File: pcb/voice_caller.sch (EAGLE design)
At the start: 22 parts, among them IC1 PRO_MICRO, IC2 AT45DB321D-S, IC3 78L12SMD, K4 G6J-2P-Y

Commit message: All but switches
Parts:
- added C7: (no value), rcl:C-EUC1206K
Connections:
- net +3V3: now also C7.1
- net GND: now also C7.2
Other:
- moved on the sheet: C1, C2, C3
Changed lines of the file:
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@@
 <part name="R7" library="rcl" deviceset="R-EU_" device="M1206" value="1k"/>
 <part name="P+3" library="supply1" deviceset="+5V" device=""/>
+<part name="C7" library="rcl" deviceset="C-EU" device="C1206K"/>
+<part name="GND11" library="supply1" deviceset="GND" device=""/>
+<part name="+3V1" library="supply1" deviceset="+3V3" device=""/>
 </parts>
 <sheets>
@@
 </plain>
 <instances>
-<instance part="+8V" gate="VCC" x="25.4" y="99.06"/>
-<instance part="GND1" gate="1" x="25.4" y="81.28"/>
+<instance part="+8V" gate="VCC" x="147.32" y="149.86"/>
+<instance part="GND1" gate="1" x="147.32" y="132.08"/>
 <instance part="CONN_MIC" gate="G$1" x="-30.48" y="50.8" rot="MR0"/>
 <instance part="CONN_RADIO" gate="G$1" x="2.54" y="50.8"/>
-<instance part="P+2" gate="1" x="40.64" y="99.06"/>
-<instance part="GND2" gate="1" x="40.64" y="81.28"/>
-<instance part="C1" gate="G$1" x="25.4" y="91.44"/>
-<instance part="C2" gate="G$1" x="40.64" y="91.44"/>
+<instance part="P+2" gate="1" x="78.74" y="157.48"/>
+<instance part="GND2" gate="1" x="78.74" y="139.7"/>
+<instance part="C1" gate="G$1" x="147.32" y="142.24"/>
+<instance part="C2" gate="G$1" x="78.74" y="149.86"/>
 <instance part="IC2" gate="G$1" x="157.48" y="68.58"/>
-<instance part="C3" gate="G$1" x="48.26" y="91.44"/>
-<instance part="P+1" gate="1" x="48.26" y="99.06"/>
-<instance part="GND3" gate="1" x="48.26" y="81.28"/>
+<instance part="C3" gate="G$1" x="167.64" y="142.24"/>
+<instance part="P+1" gate="1" x="167.64" y="149.86"/>
+<instance part="GND3" gate="1" x="167.64" y="132.08"/>
 <instance part="IC3" gate="G$1" x="154.94" y="119.38"/>
 <instance part="R1" gate="G$1" x="-15.24" y="99.06"/>
@@
 <instance part="R7" gate="G$1" x="81.28" y="53.34"/>
 <instance part="P+3" gate="1" x="93.98" y="76.2"/>
+<instance part="C7" gate="G$1" x="190.5" y="68.58"/>
+<instance part="GND11" gate="1" x="190.5" y="58.42"/>
+<instance part="+3V1" gate="G$1" x="190.5" y="76.2"/>
 </instances>
 <busses>
@@
 <pinref part="P+2" gate="1" pin="+5V"/>
 <pinref part="C2" gate="G$1" pin="1"/>
-<wire x1="40.64" y1="93.98" x2="40.64" y2="96.52" width="0.1524" layer="91"/>
+<wire x1="78.74" y1="152.4" x2="78.74" y2="154.94" width="0.1524" layer="91"/>
 </segment>
 <segment>
 <pinref part="C3" gate="G$1" pin="1"/>
 <pinref part="P+1" gate="1" pin="+5V"/>
-<wire x1="48.26" y1="96.52" x2="48.26" y2="93.98" width="0.1524" layer="91"/>
+<wire x1="167.64" y1="147.32" x2="167.64" y2="144.78" width="0.1524" layer="91"/>
 </segment>
 <segment>
@@
 <pinref part="GND1" gate="1" pin="GND"/>
 <pinref part="C1" gate="G$1" pin="2"/>
-<wire x1="25.4" y1="83.82" x2="25.4" y2="86.36" width="0.1524" layer="91"/>
+<wire x1="147.32" y1="134.62" x2="147.32" y2="137.16" width="0.1524" layer="91"/>
 </segment>
 <segment>
 <pinref part="GND2" gate="1" pin="GND"/>
 <pinref part="C2" gate="G$1" pin="2"/>
-<wire x1="40.64" y1="83.82" x2="40.64" y2="86.36" width="0.1524" layer="91"/>
+<wire x1="78.74" y1="142.24" x2="78.74" y2="144.78" width="0.1524" layer="91"/>
 </segment>
 <segment>
@@
 <pinref part="C3" gate="G$1" pin="2"/>
 <pinref part="GND3" gate="1" pin="GND"/>
-<wire x1="48.26" y1="83.82" x2="48.26" y2="86.36" width="0.1524" layer="91"/>
+<wire x1="167.64" y1="134.62" x2="167.64" y2="137.16" width="0.1524" layer="91"/>
 </segment>
 <segment>
@@
 <wire x1="93.98" y1="45.72" x2="93.98" y2="48.26" width="0.1524" layer="91"/>
 </segment>
+<segment>
+<pinref part="GND11" gate="1" pin="GND"/>
+<pinref part="C7" gate="G$1" pin="2"/>
+<wire x1="190.5" y1="60.96" x2="190.5" y2="63.5" width="0.1524" layer="91"/>
+</segment>
 </net>
 <net name="MOSI" class="0">
@@
 <pinref part="+8V" gate="VCC" pin="VCC"/>
 <pinref part="C1" gate="G$1" pin="1"/>
-<wire x1="25.4" y1="93.98" x2="25.4" y2="96.52" width="0.1524" layer="91"/>
+<wire x1="147.32" y1="144.78" x2="147.32" y2="147.32" width="0.1524" layer="91"/>
 </segment>
 </net>
@@
 <label x="175.26" y="66.04" size="1.016" layer="95" xref="yes"/>
 </segment>
-</net>
+<segment>
+<pinref part="C7" gate="G$1" pin="1"/>
+<wire x1="190.5" y1="71.12" x2="190.5" y2="73.66" width="0.1524" layer="91"/>
+<pinref part="+3V1" gate="G$1" pin="+3V3"/>
+</segment>
+</net>

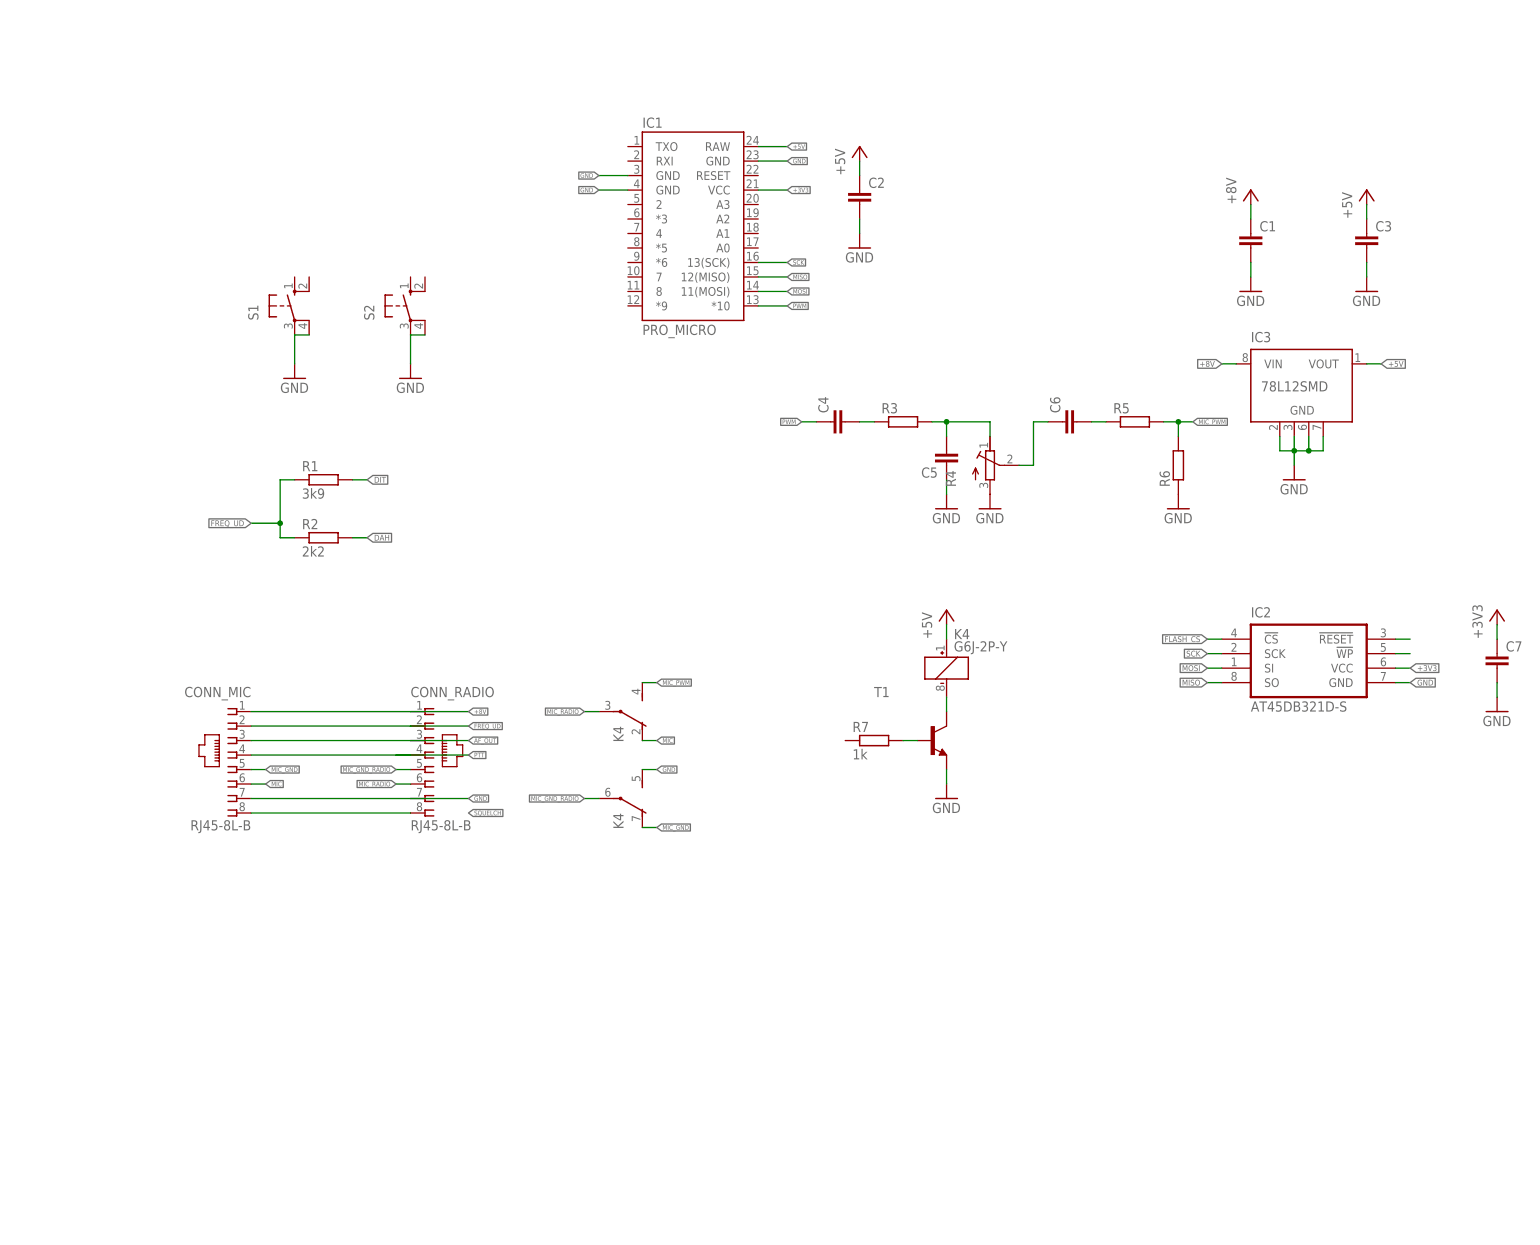
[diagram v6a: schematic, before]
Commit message: Buttons and bistable relay added, PTT thing is missing.
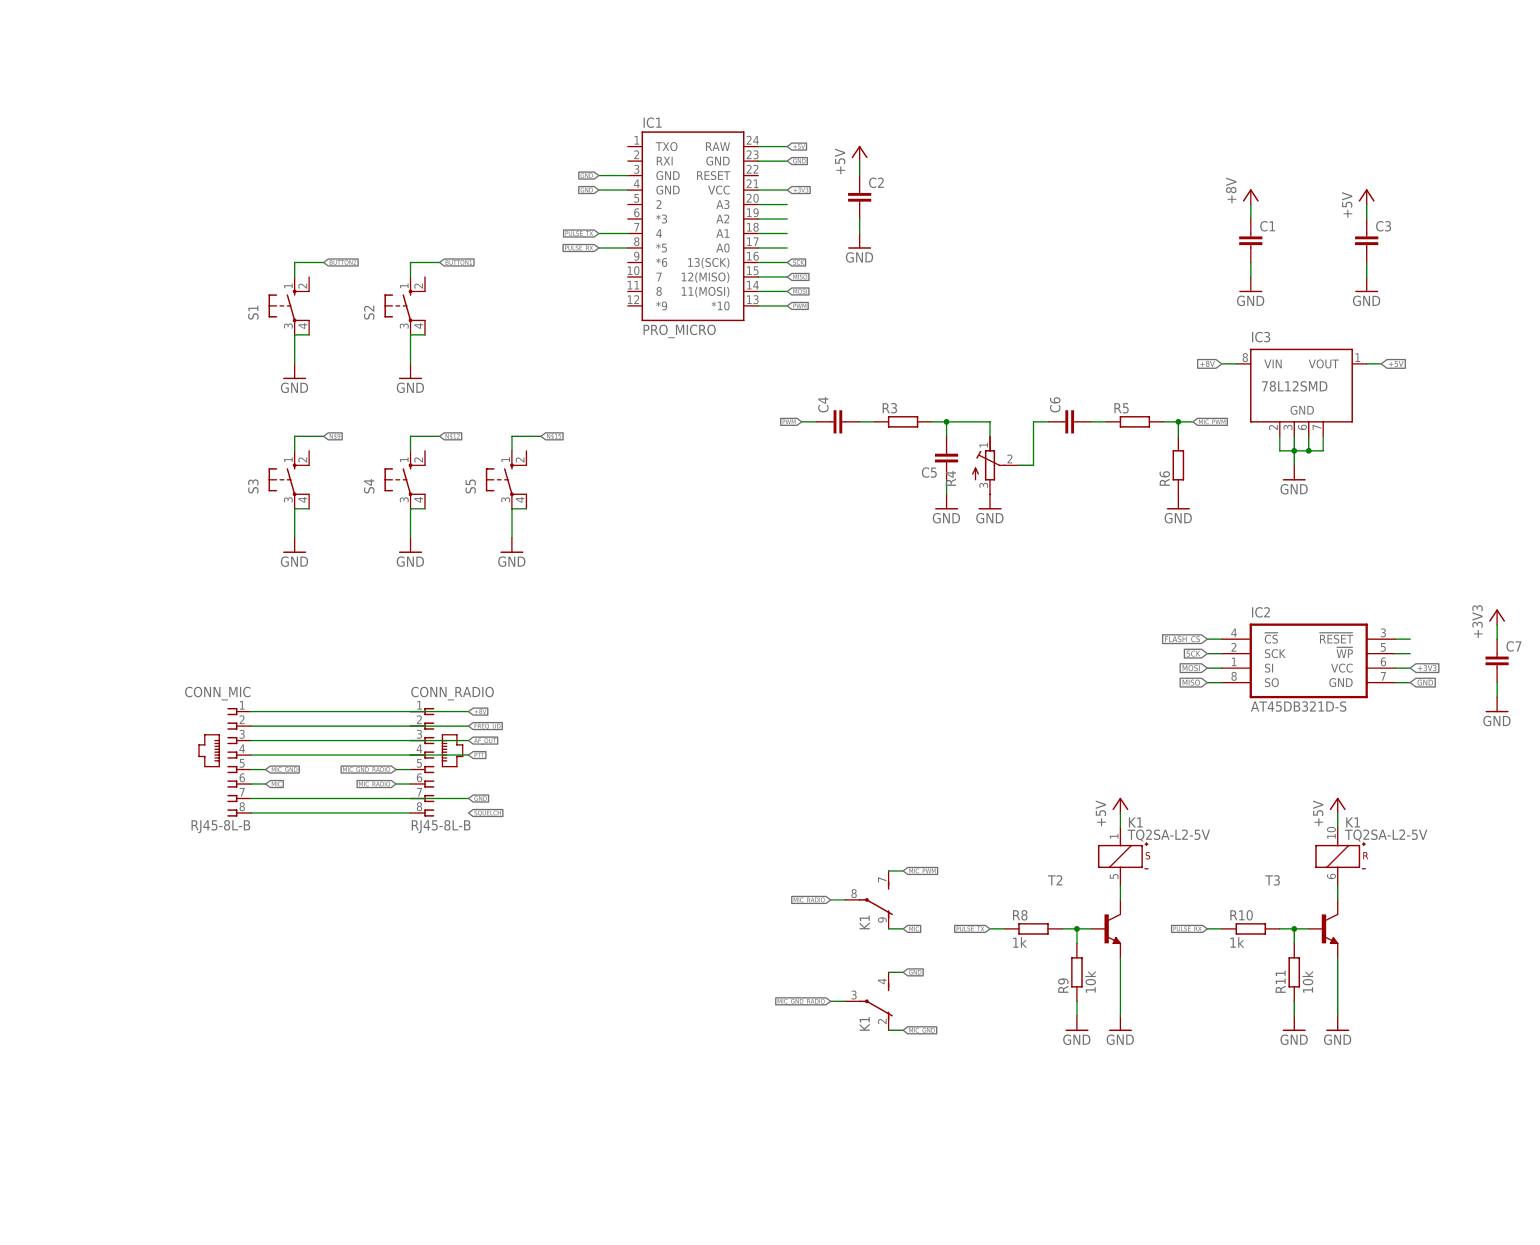
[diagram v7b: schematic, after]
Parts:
- removed K4: G6J-2P-Y, relay:G6J-2P-Y
- removed R1: 3k9, rcl:R-EU_M1206
- removed R2: 2k2, rcl:R-EU_M1206
- removed R7: 1k, rcl:R-EU_M1206
- removed T1: (no value), transistor:MMBT3904LT1-NPN-SOT23-BEC
- added K1: TQ2SA-L2-5V, relay:TQ2SA-L2-5V
- added R10, R8: 1k, rcl:R-EU_M1206
- added R11, R9: 10k, rcl:R-EU_M1206
- added S3, S4, S5: (no value), switch-omron:10-XX
- added T2, T3: (no value), transistor:MMBT3904LT1-NPN-SOT23-BEC
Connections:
- removed net DAH: R2.2
- removed net DIT: R1.2
- new net BUTTON1: S2.S
- new net BUTTON2: S1.S
- new net N$10: K1S.-, T2.C
- new net N$11: R8.2, R9.2, T2.B
- new net N$12: S4.S
- new net N$13: K1R.-, T3.C
- new net N$14: R10.2, R11.2, T3.B
- new net N$15: S5.S
- new net N$16: IC1.A1
- new net N$17: IC1.A0
- new net PULSE_RX: IC1.*5, R10.1
- new net PULSE_TX: IC1.4, R8.1
- net +5V: now also K1R.+, K1S.+; no longer K41.+
- net FREQ_UD: no longer R1.1, R2.1
- net GND: now also K11.S, R11.1, R9.1, S3.P, S3.P1, S4.P, S4.P1, S5.P, S5.P1, T2.E, T3.E; no longer K43.S, T1.E
- net MIC: now also K12.O; no longer K42.O
- net MIC_GND: now also K11.O; no longer K43.O
- net MIC_GND_RADIO: now also K11.P; no longer K43.P
- net MIC_PWM: now also K12.S; no longer K42.S
- net MIC_RADIO: now also K12.P; no longer K42.P
- net N$4: now also IC1.A3; no longer K41.-, T1.C
- net N$5: now also IC1.A2; no longer CONN_RADIO.4
- net N$9: now also S3.S; no longer R7.2, T1.B
- net PTT: now also CONN_RADIO.4
